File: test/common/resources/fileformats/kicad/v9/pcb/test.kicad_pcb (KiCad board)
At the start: 2 copper layers, 4 parts

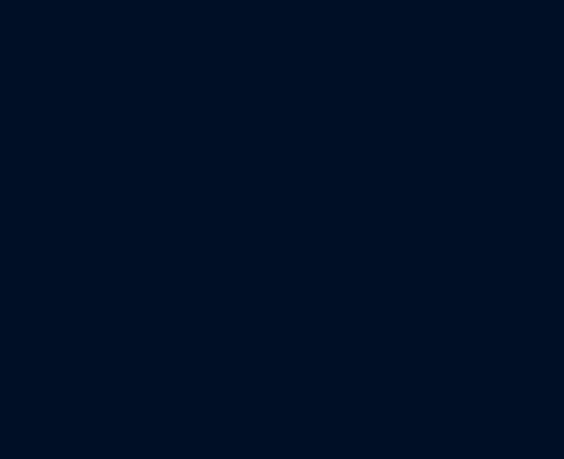
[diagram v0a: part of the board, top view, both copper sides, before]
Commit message: Restore Atopile Local 0.2 on pinned 0.15.9 sources
Import the publicly distributed atopile 0.15.9 PyPI source release as the
compiler/UI baseline, retaining upstream main as its historical parent.
PyPI source SHA256: 681cc1e123646dd133de31b631aedaf4eaac88682613b4f82d1da4b3ef8b4e8e.

Revive the local VS Code extension with a separate identity and launcher,
isolated state, bundled visualization assets, and provider settings. Bridge
the existing Atopile tool harness to a natively signed-in Codex app-server
for ChatGPT-plan use, retaining direct API providers as explicit options.
Include local part import, layout tools, packaging/runtime setup and tests.

Preserve upstream licensing, restored GitHub metadata and source notices.
Exclude local environments, generated webview bundles and personal QA paths.
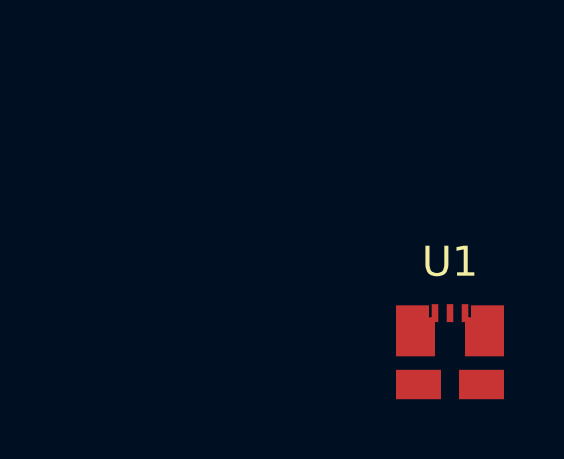
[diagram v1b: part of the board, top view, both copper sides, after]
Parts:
- added U1: TPSM863257, TestLib:TPSM863257_like, F.Cu at (120.0, 100.0)
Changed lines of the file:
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@@
 		)
+	)
+	(footprint "TestLib:TPSM863257_like"
+		(layer "F.Cu")
+		(at 120 100)
+		(property "Reference" "U1"
+			(at 0 -3 0)
+			(layer "F.SilkS")
+			(effects
+				(font
+					(size 1 1)
+					(thickness 0.15)
+				)
+			)
+		)
+		(property "Value" "TPSM863257"
+			(at 0 3 0)
+			(layer "F.Fab")
+			(effects
+				(font
+					(size 1 1)
+					(thickness 0.15)
+				)
+			)
+		)
+		(property "Datasheet" ""
+			(at 0 0 0)
+			(layer "F.Fab")
+			(hide yes)
+			(effects
+				(font
+					(size 1.27 1.27)
+					(thickness 0.15)
+				)
+			)
+		)
+		(property "Description" ""
+			(at 0 0 0)
+			(layer "F.Fab")
+			(hide yes)
+			(effects
+				(font
+					(size 1.27 1.27)
+					(thickness 0.15)
+				)
+			)
+		)
+		(attr smd)
+		(pad "1" smd custom
+			(at -0.97 -0.7)
+			(size 0.01 0.01)
+			(layers "F.Cu" "F.Paste" "F.Mask")
+			(options
+				(clearance outline)
+				(anchor circle)
+			)
+			(primitives
+				(gr_poly
+					(pts
+						(xy -0.83 -0.85) (xy 0.27 -0.85) (xy 0.27 -0.45) (xy 0.47 -0.45) (xy 0.47 0.85) (xy -0.83 0.85)
+					)
+					(fill yes)
+				)
+			)
+		)
+		(pad "2" smd custom
+			(at -1.05 1.29)
+			(size 0.01 0.01)
+			(layers "F.Cu" "F.Paste" "F.Mask")
+			(options
+				(clearance outline)
+				(anchor circle)
+			)
+			(primitives
+				(gr_poly
+					(pts
+						(xy -0.75 -0.69) (xy 0.75 -0.69) (xy 0.75 0.29) (xy -0.75 0.29)
+					)
+					(fill yes)
+				)
+			)
+		)
+		(pad "3" smd custom
+			(at 1.05 1.29)
+			(size 0.01 0.01)
+			(layers "F.Cu" "F.Paste" "F.Mask")
+			(options
+				(clearance outline)
+				(anchor circle)
+			)
+			(primitives
+				(gr_poly
+					(pts
+						(xy -0.75 -0.69) (xy 0.75 -0.69) (xy 0.75 0.29) (xy -0.75 0.29)
+					)
+					(fill yes)
+				)
+			)
+		)
+		(pad "4" smd custom
+			(at 0.98 -0.7)
+			(size 0.01 0.01)
+			(layers "F.Cu" "F.Paste" "F.Mask")
+			(options
+				(clearance outline)
+				(anchor circle)
+			)
+			(primitives
+				(gr_poly
+					(pts
+						(xy -0.48 -0.85) (xy 0.82 -0.85) (xy 0.82 0.85) (xy -0.48 0.85) (xy -0.48 -0.45) (xy -0.28 -0.45)
+						(xy -0.28 -0.85)
+					)
+					(fill yes)
+				)
+			)
+		)
+		(pad "5" smd rect
+			(at -0.5 -1.29)
+			(size 0.22 0.6)
+			(layers "F.Cu" "F.Paste" "F.Mask")
+		)
+		(pad "6" smd rect
+			(at 0 -1.29)
+			(size 0.22 0.6)
+			(layers "F.Cu" "F.Paste" "F.Mask")
+		)
+		(pad "7" smd rect
+			(at 0.5 -1.29)
+			(size 0.22 0.6)
+			(layers "F.Cu" "F.Paste" "F.Mask")
+		)
+		(embedded_fonts no)
 	)
 	(gr_text "Multi-line text\nnewline\nreturn\r\nsingle backslash \\\ndouble backslash \\\\\ntab>	<tab"
